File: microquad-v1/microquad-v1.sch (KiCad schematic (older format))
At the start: 6 parts, among them SW1 SERIAL, SW2 POWER, SW3 RESET, U1 ATMEGA328PB

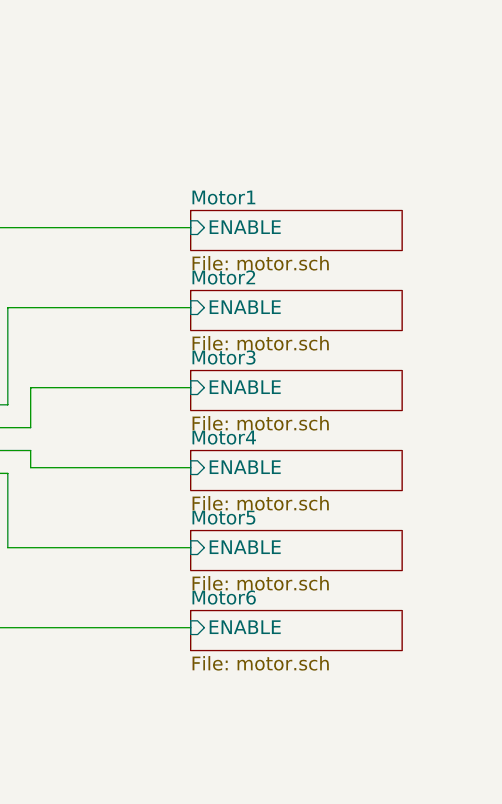
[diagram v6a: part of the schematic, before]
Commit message: Fixed VBAT connections
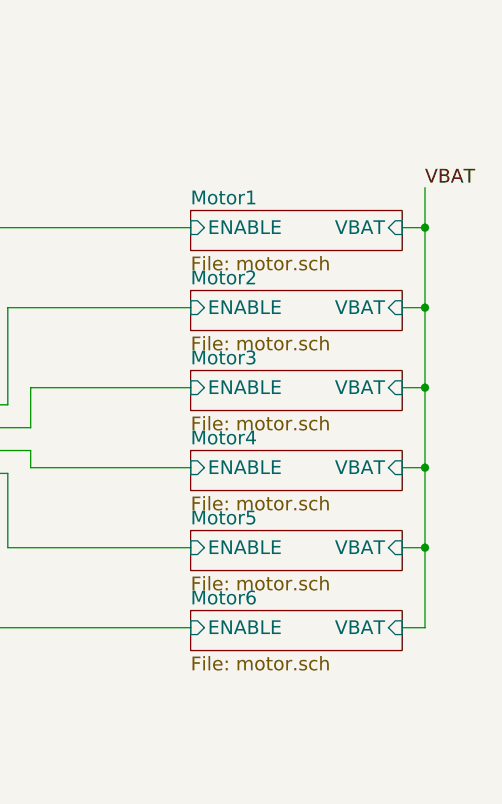
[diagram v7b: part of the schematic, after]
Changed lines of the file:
@@
 F1 "motor.sch" 60
 F2 "ENABLE" I L 8350 3375 60
+F3 "VBAT" I R 9275 3375 60
 $EndSheet
 $Sheet
@@
 F1 "motor.sch" 60
 F2 "ENABLE" I L 8350 3725 60
+F3 "VBAT" I R 9275 3725 60
 $EndSheet
 $Sheet
@@
 F1 "motor.sch" 60
 F2 "ENABLE" I L 8350 4075 60
+F3 "VBAT" I R 9275 4075 60
 $EndSheet
 $Sheet
@@
 F1 "motor.sch" 60
 F2 "ENABLE" I L 8350 4425 60
+F3 "VBAT" I R 9275 4425 60
 $EndSheet
 $Sheet
@@
 F1 "motor.sch" 60
 F2 "ENABLE" I L 8350 4775 60
+F3 "VBAT" I R 9275 4775 60
 $EndSheet
 $Sheet
@@
 F1 "motor.sch" 60
 F2 "ENABLE" I L 8350 5125 60
+F3 "VBAT" I R 9275 5125 60
 $EndSheet
 Wire Wire Line
@@
 Wire Wire Line
 	7450 5125 8350 5125
+Text Label 9375 3200 0    60   ~ 0
+VBAT
+Wire Wire Line
+	9375 3200 9375 5125
+Wire Wire Line
+	9375 5125 9275 5125
+Wire Wire Line
+	9275 4775 9375 4775
+Connection ~ 9375 4775
+Wire Wire Line
+	9275 4425 9375 4425
+Connection ~ 9375 4425
+Wire Wire Line
+	9275 3375 9375 3375
+Connection ~ 9375 3375
+Wire Wire Line
+	9275 3725 9375 3725
+Connection ~ 9375 3725
+Wire Wire Line
+	9275 4075 9375 4075
+Connection ~ 9375 4075
 $EndSCHEMATC

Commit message: Ladybug is satisfied
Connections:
- net Motor1/ENABLE: now also U1.14 (PB2/OC1B); no longer U1.32 (PD2/OC3B/OC4B)
- net Motor2/ENABLE: now also U1.13 (PB1/OC1A); no longer U1.31 (PD1/OC4A)
- net Motor4/ENABLE: now also U1.32 (PD2/OC3B/OC4B); no longer U1.14 (PB2/OC1B)
- net Motor5/ENABLE: now also U1.31 (PD1/OC4A); no longer U1.13 (PB1/OC1A)
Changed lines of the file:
@@
 	1800 2450 1550 2450
 $Sheet
-S 8350 3300 925  175
+S 8350 4350 925  175
 U 59F7E793
 F0 "Motor1" 60
 F1 "motor.sch" 60
-F2 "ENABLE" I L 8350 3375 60
-F3 "VBAT" I R 9275 3375 60
+F2 "ENABLE" I L 8350 4425 60
+F3 "VBAT" I R 9275 4425 60
 $EndSheet
 $Sheet
-S 8350 3650 925  175
+S 8350 4700 925  175
 U 59F7F6E8
 F0 "Motor2" 60
 F1 "motor.sch" 60
-F2 "ENABLE" I L 8350 3725 60
-F3 "VBAT" I R 9275 3725 60
+F2 "ENABLE" I L 8350 4775 60
+F3 "VBAT" I R 9275 4775 60
 $EndSheet
 $Sheet
@@
 $EndSheet
 $Sheet
-S 8350 4350 925  175
+S 8350 3300 925  175
 U 59F7FC61
 F0 "Motor4" 60
 F1 "motor.sch" 60
-F2 "ENABLE" I L 8350 4425 60
-F3 "VBAT" I R 9275 4425 60
+F2 "ENABLE" I L 8350 3375 60
+F3 "VBAT" I R 9275 3375 60
 $EndSheet
 $Sheet
-S 8350 4700 925  175
+S 8350 3650 925  175
 U 59F7FFA1
 F0 "Motor5" 60
 F1 "motor.sch" 60
-F2 "ENABLE" I L 8350 4775 60
-F3 "VBAT" I R 9275 4775 60
+F2 "ENABLE" I L 8350 3725 60
+F3 "VBAT" I R 9275 3725 60
 $EndSheet
 $Sheet
